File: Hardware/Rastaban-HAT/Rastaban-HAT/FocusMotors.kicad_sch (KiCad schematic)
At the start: 9 parts, among them U6 TMC2208_Carrier, U7 DRV8838 POLOLU, U8 TLV1117-33

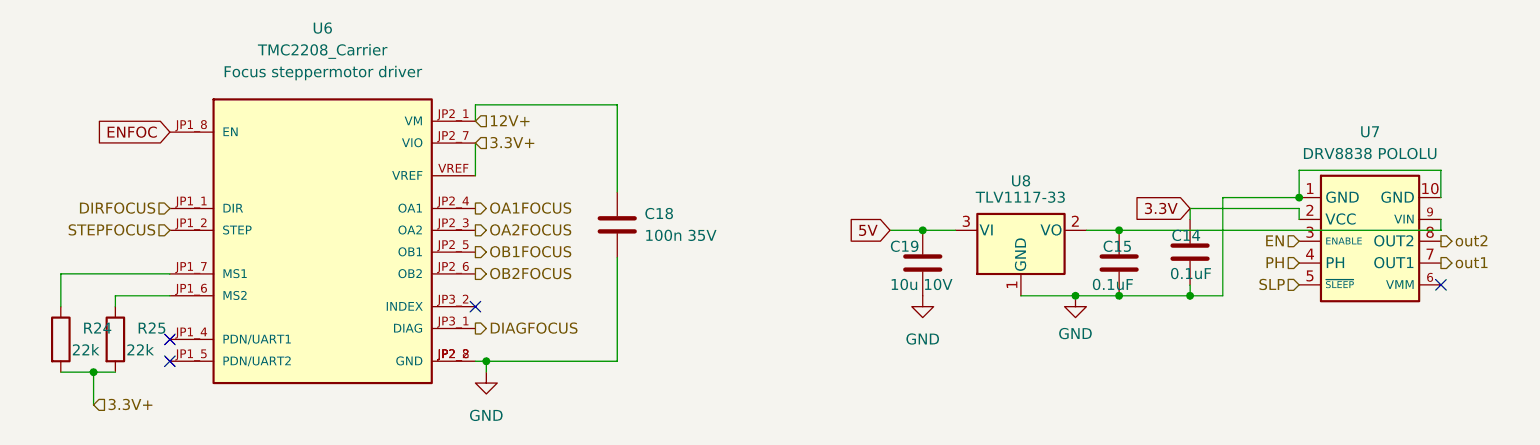
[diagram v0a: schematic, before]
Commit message: Heavily improved symbol text placements
all texts are now readable
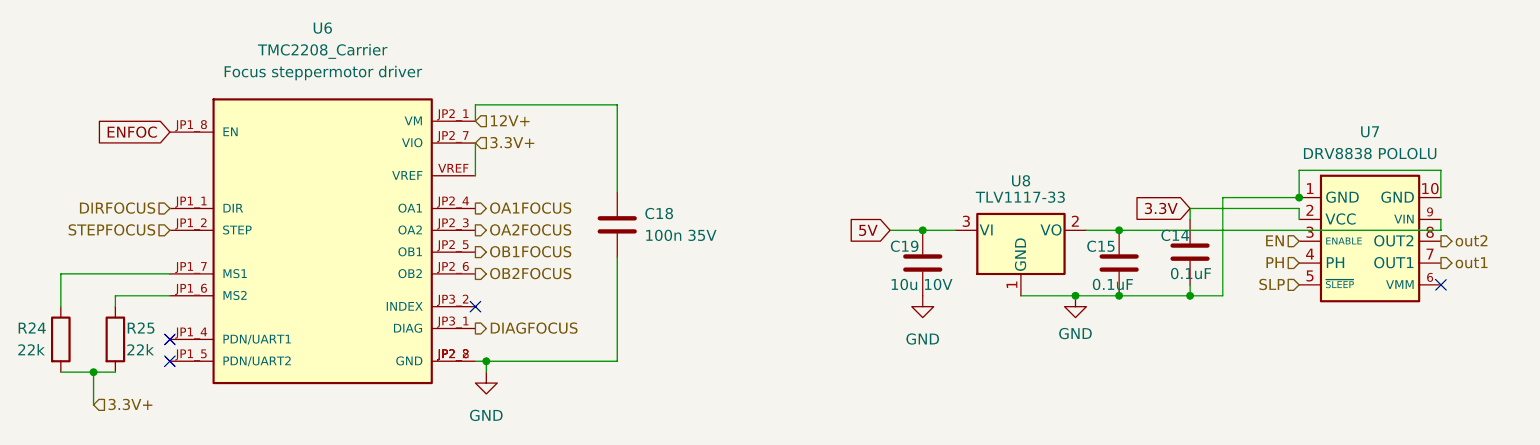
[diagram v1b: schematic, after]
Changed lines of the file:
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@@
   (symbol (lib_id "Device:C") (at 193.04 111.125 180) (unit 1)
     (in_bom yes) (on_board yes)
-    (property "Reference" "C15" (id 0) (at 191.135 109.22 0)
+    (property "Reference" "C15" (id 0) (at 189.23 109.22 0)
       (effects (font (size 1.27 1.27)) (justify right))
     )
@@
   (symbol (lib_id "Device:C") (at 201.295 109.855 0) (unit 1)
     (in_bom yes) (on_board yes)
-    (property "Reference" "C14" (id 0) (at 202.565 107.95 0)
+    (property "Reference" "C14" (id 0) (at 201.295 107.95 0)
       (effects (font (size 1.27 1.27)) (justify right))
     )
@@
   (symbol (lib_id "Device:R") (at 69.85 120.015 0) (unit 1)
     (in_bom yes) (on_board yes)
-    (property "Reference" "R24" (id 0) (at 72.39 118.7449 0)
+    (property "Reference" "R24" (id 0) (at 64.77 118.745 0)
       (effects (font (size 1.27 1.27)) (justify left))
     )
-    (property "Value" "22k" (id 1) (at 71.12 121.285 0)
+    (property "Value" "22k" (id 1) (at 64.77 121.285 0)
       (effects (font (size 1.27 1.27)) (justify left))
     )
@@
   (symbol (lib_id "Device:R") (at 76.2 120.015 0) (unit 1)
     (in_bom yes) (on_board yes)
-    (property "Reference" "R25" (id 0) (at 78.74 118.7449 0)
+    (property "Reference" "R25" (id 0) (at 77.47 118.745 0)
       (effects (font (size 1.27 1.27)) (justify left))
     )

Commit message: enh layout
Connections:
- net 3.3V is gone; now on net 3.3V+: C14.1, U7.2 (VCC)
- net 5V renamed 5V+
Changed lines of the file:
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@@
   (title_block
     (title "Rastaban-HAT")
+    (date "2022-09-27")
     (rev "1.1")
     (company "HAN")
@@
     (stroke (width 0) (type default) (color 0 0 0 0))
   )
-  (global_label "3.3V" (shape input) (at 201.295 104.775 180) (fields_autoplaced)
+  (global_label "3.3V+" (shape input) (at 201.295 104.775 180) (fields_autoplaced)
     (effects (font (size 1.27 1.27)) (justify right))
-    (property "Intersheet References" "${INTERSHEET_REFS}" (id 0) (at 194.7695 104.6956 0)
+    (property "Intersheet References" "${INTERSHEET_REFS}" (id 0) (at 193.1971 104.6956 0)
       (effects (font (size 1.27 1.27)) (justify right) hide)
     )
   )
-  (global_label "5V" (shape input) (at 166.37 107.315 180) (fields_autoplaced)
+  (global_label "5V+" (shape input) (at 166.37 107.315 180) (fields_autoplaced)
     (effects (font (size 1.27 1.27)) (justify right))
-    (property "Intersheet References" "${INTERSHEET_REFS}" (id 0) (at 161.6588 107.3944 0)
+    (property "Intersheet References" "${INTERSHEET_REFS}" (id 0) (at 160.0864 107.2356 0)
       (effects (font (size 1.27 1.27)) (justify right) hide)
     )

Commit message: Schematic v1.2
added johan brussen's advice
written software for stepper motor drivers
test report written.
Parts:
- added C24: 100nF, symbol Device:C
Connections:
- net 3.3V+: now also C24.1, C24.2
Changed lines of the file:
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@@
     (title "Rastaban-HAT")
     (date "2022-09-27")
-    (rev "1.1")
+    (rev "1.2")
     (company "HAN")
     (comment 1 "Casper R. Tak")
@@
   (junction (at 119.38 122.555) (diameter 0) (color 0 0 0 0)
   )
+  (junction (at 118.11 100.965) (diameter 0) (color 0 0 0 0)
+  )
   (junction (at 193.04 107.315) (diameter 0) (color 0 0 0 0)
   )
   (junction (at 213.995 103.505) (diameter 0) (color 0 0 0 0)
+  )
+  (junction (at 118.11 97.155) (diameter 0) (color 0 0 0 0)
   )
   (junction (at 170.18 107.315) (diameter 0) (color 0 0 0 0)
@@
     (stroke (width 0) (type default) (color 0 0 0 0))
   )
+  (wire (pts (xy 118.11 102.87) (xy 126.365 102.87))
+    (stroke (width 0) (type default) (color 0 0 0 0))
+  )
   (wire (pts (xy 201.295 113.665) (xy 201.295 114.935))
     (stroke (width 0) (type default) (color 0 0 0 0))
@@
     (stroke (width 0) (type default) (color 0 0 0 0))
   )
+  (wire (pts (xy 118.11 97.155) (xy 118.11 95.25))
+    (stroke (width 0) (type default) (color 0 0 0 0))
+  )
   (wire (pts (xy 119.38 123.825) (xy 119.38 122.555))
     (stroke (width 0) (type default) (color 0 0 0 0))
@@
     (stroke (width 0) (type default) (color 0 0 0 0))
   )
+  (wire (pts (xy 118.11 100.965) (xy 118.11 102.87))
+    (stroke (width 0) (type default) (color 0 0 0 0))
+  )
   (wire (pts (xy 82.55 114.935) (xy 76.2 114.935))
     (stroke (width 0) (type default) (color 0 0 0 0))
@@
   )
   (wire (pts (xy 230.505 106.045) (xy 230.505 107.315))
+    (stroke (width 0) (type default) (color 0 0 0 0))
+  )
+  (wire (pts (xy 118.11 95.25) (xy 126.365 95.25))
     (stroke (width 0) (type default) (color 0 0 0 0))
   )
@@
       (effects (font (size 1.27 1.27)) hide)
     )
+    (pin "1")
+    (pin "2")
+  )
+  (symbol (lib_id "Device:C") (at 126.365 99.06 0) (unit 1)
+    (in_bom yes) (on_board yes) (fields_autoplaced)
+    (property "Reference" "C24" (id 0) (at 129.54 97.7899 0)
+      (effects (font (size 1.27 1.27)) (justify left))
+    )
+    (property "Value" "100nF" (id 1) (at 129.54 100.3299 0)
+      (effects (font (size 1.27 1.27)) (justify left))
+    )
+    (property "Footprint" "" (id 2) (at 127.3302 102.87 0)
+      (effects (font (size 1.27 1.27)) hide)
+    )
+    (property "Datasheet" "~" (id 3) (at 126.365 99.06 0)
+      (effects (font (size 1.27 1.27)) hide)
+    )

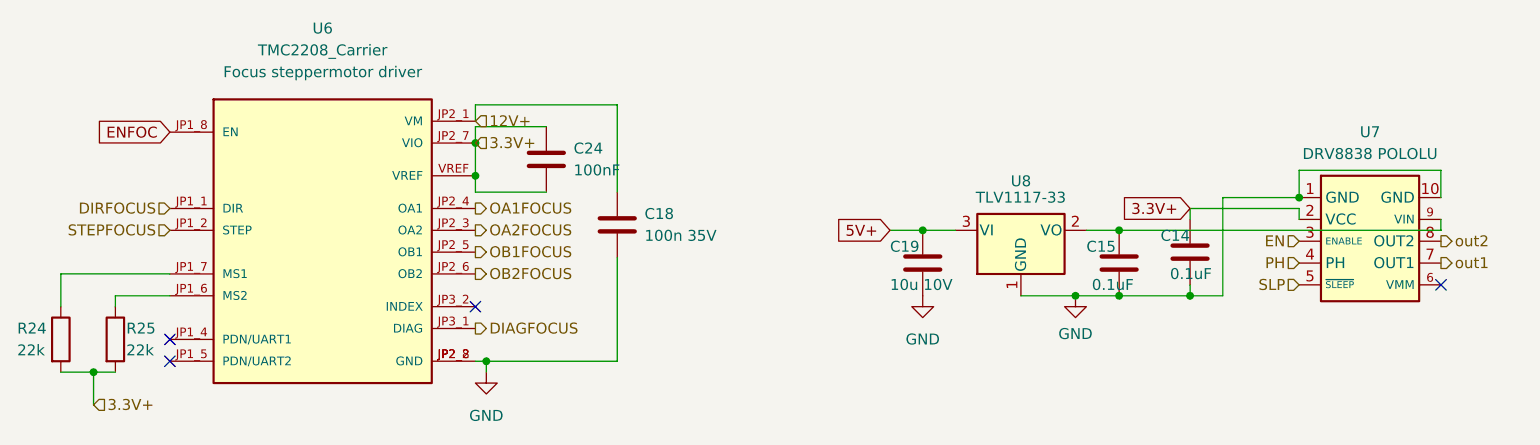
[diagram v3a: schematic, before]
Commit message: added new libarries and jlcpcb part plugin
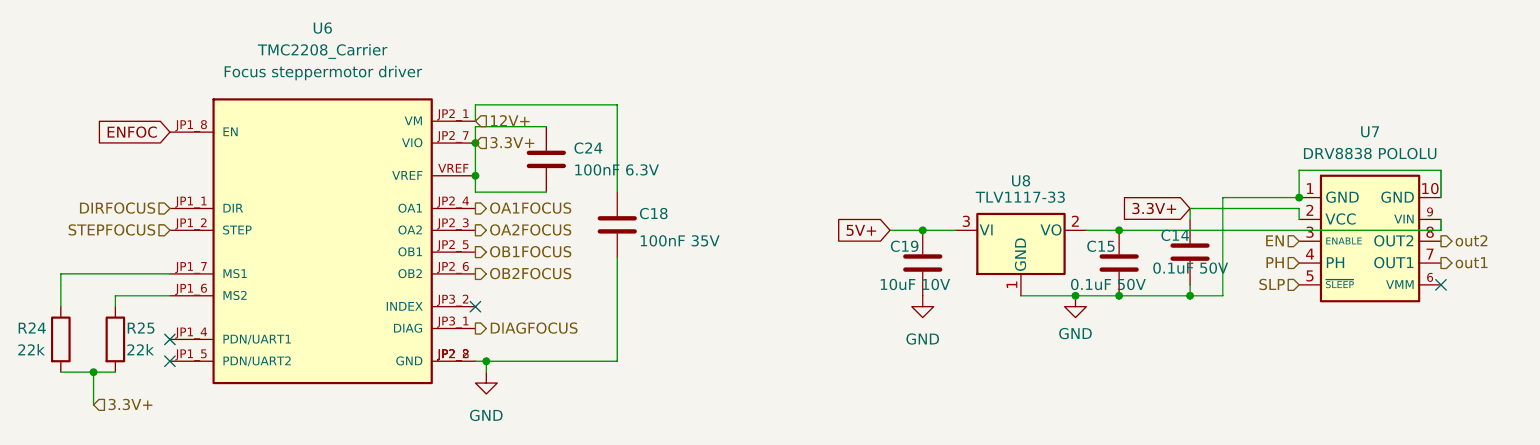
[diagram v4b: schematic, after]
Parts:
- C14, C15: value 0.1uF -> 0.1uF 50V; footprint Capacitor_SMD:C_1206_3216Metric_Pad1.33x1.80mm_HandSolder -> Capacitor_SMD:C_0805_2012Metric_Pad1.18x1.45mm_HandSolder
- C18: value 100n 35V -> 100nF 35V; footprint (none) -> Capacitor_THT:C_Radial_D6.3mm_H11.0mm_P2.50mm; Manufacturer_Part_Number (none) -> C525005
- C19: value 10u 10V -> 10uF 10V; footprint (none) -> Capacitor_THT:C_Radial_D6.3mm_H11.0mm_P2.50mm; Manufacturer_Part_Number (none) -> C513765
- C24: value 100nF -> 100nF 6.3V; footprint (none) -> Capacitor_SMD:C_0805_2012Metric_Pad1.18x1.45mm_HandSolder
- R24, R25: footprint Resistor_SMD:R_1206_3216Metric_Pad1.30x1.75mm_HandSolder -> Resistor_SMD:R_0805_2012Metric_Pad1.20x1.40mm_HandSolder
- U6: footprint Footprints:TMC2208_SILENTSTEPSTICK -> (none)
- U8: footprint (none) -> SamacSys_Parts:SOT230P700X180-4N
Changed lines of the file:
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@@
     (property "Reference" "U6" (id 0) (at 100.33 83.82 0))
     (property "Value" "TMC2208_Carrier" (id 1) (at 100.33 86.36 0))
-    (property "Footprint" "Footprints:TMC2208_SILENTSTEPSTICK" (id 2) (at 85.09 128.905 0)
+    (property "Footprint" "" (id 2) (at 85.09 128.905 0)
       (effects (font (size 1.27 1.27)) (justify left bottom) hide)
     )
@@
       (effects (font (size 1.27 1.27)) (justify right))
     )
-    (property "Value" "0.1uF" (id 1) (at 189.865 113.665 0)
-      (effects (font (size 1.27 1.27)) (justify right))
-    )
-    (property "Footprint" "Capacitor_SMD:C_1206_3216Metric_Pad1.33x1.80mm_HandSolder" (id 2) (at 192.0748 107.315 0)
+    (property "Value" "0.1uF 50V" (id 1) (at 187.325 113.665 0)
+      (effects (font (size 1.27 1.27)) (justify right))
+    )
+    (property "Footprint" "Capacitor_SMD:C_0805_2012Metric_Pad1.18x1.45mm_HandSolder" (id 2) (at 192.0748 107.315 0)
       (effects (font (size 1.27 1.27)) hide)
     )
@@
     (property "Reference" "U8" (id 0) (at 181.61 101.6 0))
     (property "Value" "TLV1117-33" (id 1) (at 181.61 103.505 0))
-    (property "Footprint" "" (id 2) (at 181.61 107.315 0)
+    (property "Footprint" "SamacSys_Parts:SOT230P700X180-4N" (id 2) (at 181.61 107.315 0)
       (effects (font (size 1.27 1.27)) hide)
     )
@@
       (effects (font (size 1.27 1.27)) (justify right))
     )
-    (property "Value" "0.1uF" (id 1) (at 203.835 112.395 0)
-      (effects (font (size 1.27 1.27)) (justify right))
-    )
-    (property "Footprint" "Capacitor_SMD:C_1206_3216Metric_Pad1.33x1.80mm_HandSolder" (id 2) (at 202.2602 113.665 0)
+    (property "Value" "0.1uF 50V" (id 1) (at 205.74 111.76 0)
+      (effects (font (size 1.27 1.27)) (justify right))
+    )
+    (property "Footprint" "Capacitor_SMD:C_0805_2012Metric_Pad1.18x1.45mm_HandSolder" (id 2) (at 202.2602 113.665 0)
       (effects (font (size 1.27 1.27)) hide)
     )
@@
   )
   (symbol (lib_id "Device:C") (at 134.62 106.68 0) (unit 1)
-    (in_bom yes) (on_board yes) (fields_autoplaced)
-    (property "Reference" "C18" (id 0) (at 137.795 105.4099 0)
-      (effects (font (size 1.27 1.27)) (justify left))
-    )
-    (property "Value" "100n 35V" (id 1) (at 137.795 107.9499 0)
-      (effects (font (size 1.27 1.27)) (justify left))
-    )
-    (property "Footprint" "" (id 2) (at 135.5852 110.49 0)
+    (in_bom yes) (on_board yes)
+    (property "Reference" "C18" (id 0) (at 137.16 105.41 0)
+      (effects (font (size 1.27 1.27)) (justify left))
+    )
+    (property "Value" "100nF 35V" (id 1) (at 137.16 108.585 0)
+      (effects (font (size 1.27 1.27)) (justify left))
+    )
+    (property "Footprint" "Capacitor_THT:C_Radial_D6.3mm_H11.0mm_P2.50mm" (id 2) (at 135.5852 110.49 0)
       (effects (font (size 1.27 1.27)) hide)
     )
     (property "Datasheet" "~" (id 3) (at 134.62 106.68 0)
+      (effects (font (size 1.27 1.27)) hide)
+    )
+    (property "LCSC Part#" "" (id 4) (at 134.62 106.68 0)
+      (effects (font (size 1.27 1.27)) hide)
+    )
+    (property "Manufacturer_Part_Number" "C525005" (id 5) (at 134.62 106.68 0)
       (effects (font (size 1.27 1.27)) hide)
     )
@@
       (effects (font (size 1.27 1.27)) (justify left))
     )
-    (property "Footprint" "Resistor_SMD:R_1206_3216Metric_Pad1.30x1.75mm_HandSolder" (id 2) (at 68.072 120.015 90)
+    (property "Footprint" "Resistor_SMD:R_0805_2012Metric_Pad1.20x1.40mm_HandSolder" (id 2) (at 68.072 120.015 90)
       (effects (font (size 1.27 1.27)) hide)
     )
@@
       (effects (font (size 1.27 1.27)) (justify left))
     )
-    (property "Value" "100nF" (id 1) (at 129.54 100.3299 0)
-      (effects (font (size 1.27 1.27)) (justify left))
-    )
-    (property "Footprint" "" (id 2) (at 127.3302 102.87 0)
+    (property "Value" "100nF 6.3V" (id 1) (at 129.54 100.3299 0)
+      (effects (font (size 1.27 1.27)) (justify left))
+    )
+    (property "Footprint" "Capacitor_SMD:C_0805_2012Metric_Pad1.18x1.45mm_HandSolder" (id 2) (at 127.3302 102.87 0)
       (effects (font (size 1.27 1.27)) hide)
     )
@@
       (effects (font (size 1.27 1.27)) (justify left))
     )
-    (property "Footprint" "Resistor_SMD:R_1206_3216Metric_Pad1.30x1.75mm_HandSolder" (id 2) (at 74.422 120.015 90)
+    (property "Footprint" "Resistor_SMD:R_0805_2012Metric_Pad1.20x1.40mm_HandSolder" (id 2) (at 74.422 120.015 90)
       (effects (font (size 1.27 1.27)) hide)
     )
@@
       (effects (font (size 1.27 1.27)) (justify left))
     )
-    (property "Value" "10u 10V" (id 1) (at 166.37 113.665 0)
-      (effects (font (size 1.27 1.27)) (justify left))
-    )
-    (property "Footprint" "" (id 2) (at 171.1452 114.935 0)
+    (property "Value" "10uF 10V" (id 1) (at 165.1 113.665 0)
+      (effects (font (size 1.27 1.27)) (justify left))
+    )
+    (property "Footprint" "Capacitor_THT:C_Radial_D6.3mm_H11.0mm_P2.50mm" (id 2) (at 171.1452 114.935 0)
       (effects (font (size 1.27 1.27)) hide)
     )
@@
       (effects (font (size 1.27 1.27)) hide)
     )
+    (property "Manufacturer_Part_Number" "C513765" (id 4) (at 170.18 111.125 0)
+      (effects (font (size 1.27 1.27)) hide)
+    )
+    (property "LCSC Part#" "" (id 5) (at 170.18 111.125 0)
+      (effects (font (size 1.27 1.27)) hide)
+    )

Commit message: updated footprints
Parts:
- U6: footprint (none) -> SnapEDA Library:MODULE_TMC2208_SILENTSTEPSTICK
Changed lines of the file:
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@@
     (property "Reference" "U6" (id 0) (at 100.33 83.82 0))
     (property "Value" "TMC2208_Carrier" (id 1) (at 100.33 86.36 0))
-    (property "Footprint" "" (id 2) (at 85.09 128.905 0)
+    (property "Footprint" "SnapEDA Library:MODULE_TMC2208_SILENTSTEPSTICK" (id 2) (at 85.09 128.905 0)
       (effects (font (size 1.27 1.27)) (justify left bottom) hide)
     )

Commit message: ERC fixed on schematic
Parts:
- U7: footprint Package_SON:WSON-8-1EP_2x2mm_P0.5mm_EP0.9x1.6mm -> (none)
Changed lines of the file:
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@@
     (property "Reference" "U7" (id 0) (at 222.25 95.885 0))
     (property "Value" "DRV8838 POLOLU" (id 1) (at 222.25 98.425 0))
-    (property "Footprint" "Package_SON:WSON-8-1EP_2x2mm_P0.5mm_EP0.9x1.6mm" (id 2) (at 226.695 130.81 0)
+    (property "Footprint" "" (id 2) (at 226.695 130.81 0)
       (effects (font (size 1.27 1.27)) hide)
     )

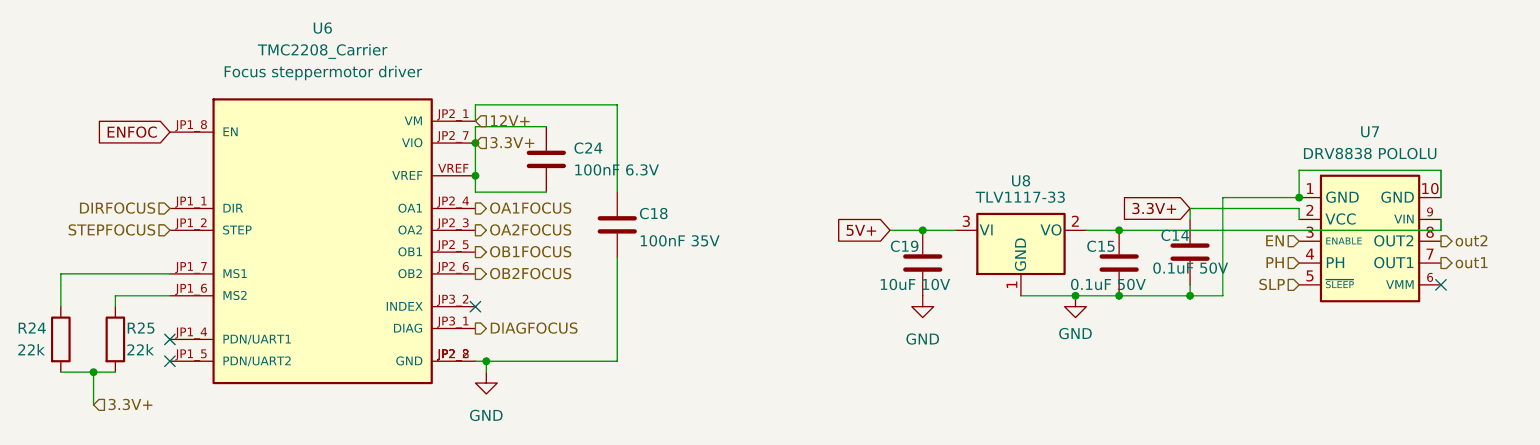
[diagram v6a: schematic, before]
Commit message: removed warnings in PCB new by fixing footprints
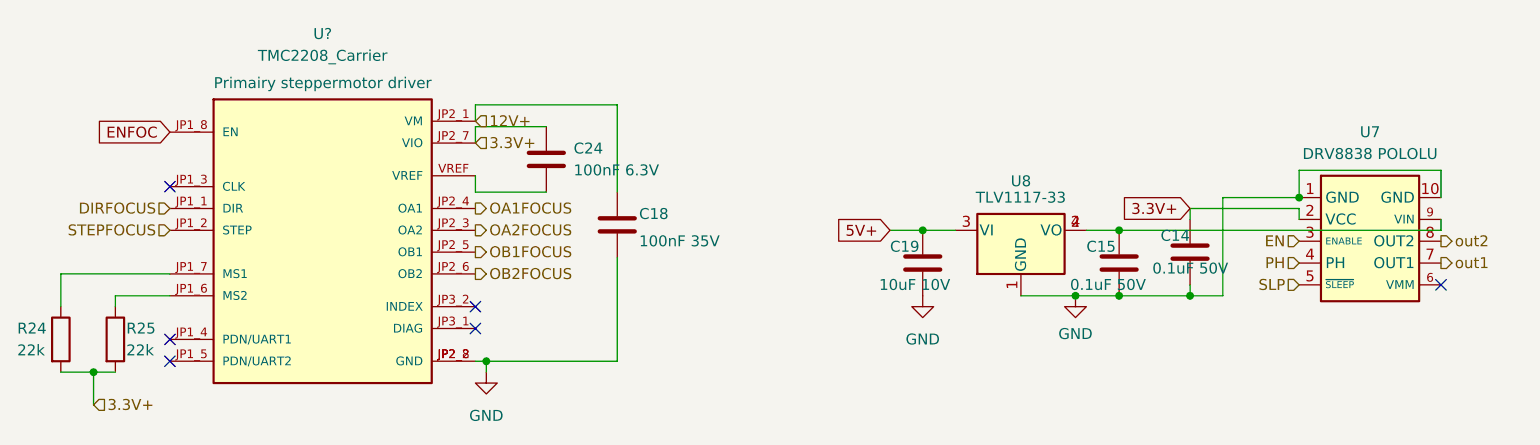
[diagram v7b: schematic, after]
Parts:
- removed U6: TMC2208_Carrier, SnapEDA Library:MODULE_TMC2208_SILENTSTEPSTICK, symbol TMC2208_SILENTSTEPSTICK:TMC2208_SILENTSTEPSTICK
- added U?: TMC2208_Carrier, SnapEDA Library:MODULE_TMC2208_SILENTSTEPSTICK, symbol TMC2208_SILENTSTEPSTICK:TMC2208_SILENTSTEPSTICK
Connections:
- net 12V+: now also U?.JP2_1 (VM)
- net 3.3V+: now also U?.JP2_7 (VIO); no longer C24.2
- net DIRFOCUS: now also U?.JP1_1 (DIR)
- net ENFOC: now also U?.JP1_8 (EN)
- net GND: now also U?.JP2_2 (GND), U?.JP2_8 (GND)
- net OA1FOCUS: now also U?.JP2_4 (OA1)
- net OA2FOCUS: now also U?.JP2_3 (OA2)
- net OB1FOCUS: now also U?.JP2_5 (OB1)
- net OB2FOCUS: now also U?.JP2_6 (OB2)
- net STEPFOCUS: now also U?.JP1_2 (STEP)
- net at R25.1: now also U?.JP1_6 (MS2)
- net at R24.1: now also U?.JP1_7 (MS1)
- net at C15.2, U7.9 (VIN), U8.2 (VO): now also U8.4 (VO)
- new net: C24.2, U?.VREF
- no-connect marks 4 -> 6
